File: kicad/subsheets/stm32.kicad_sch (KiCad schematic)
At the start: 11 parts, among them U4 STM32U575RGT6

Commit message: Finalized PMIC and added control from STM32
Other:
- note added: "DEBUG"
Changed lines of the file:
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@@
+		)
+	)
+	(text "DEBUG"
+		(exclude_from_sim no)
+		(at 196.85 62.738 0)
+		(effects
+			(font
+				(size 1.27 1.27)
+			)
+			(justify left)
 		)
 	)
 	(text "RK3566 \nCTRL/DATA"
 		(exclude_from_sim no)
-		(at 202.946 40.894 0)
+		(at 205.486 78.486 0)
 		(effects
 			(font
@@
 	(text "PMIC\n"
 		(exclude_from_sim no)
-		(at 145.542 43.434 0)
+		(at 148.082 81.026 0)
 		(effects
 			(font
@@
 	(text "IMU"
 		(exclude_from_sim no)
-		(at 195.58 64.008 0)
+		(at 198.12 101.6 0)
 		(effects
 			(font
@@
 	(text "FC CTRL"
 		(exclude_from_sim no)
-		(at 153.162 64.516 0)
+		(at 155.702 102.108 0)
 		(effects
 			(font
@@
 	)
 	(image
-		(at 175.26 44.45)
+		(at 177.8 82.042)
 		(data "iVBORw0KGgoAAAANSUhEUgAAAygAAAMVCAIAAAATckfVAAAAA3NCSVQICAjb4U/gAAAgAElEQVR4"
 			"nOzdd1wT9/8H8M8FSEhkBgS1ggFUHLgQ0VYUFATcrbVVXLUuat3a8i0oFQdu0ap11rZWW61aa7EO"

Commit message: Annotations + minor tweaks
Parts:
- renumbered C44 to C41, C45 to C42, C46 to C43, C47 to C44, C48 to C45, C49 to C46, C50 to C47, C51 to C48, C52 to C49, R27 to R26

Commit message: Annotations + minor tweaks
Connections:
- net GND: now also U4.31 (VSS), U4.47 (VSS), U4.63 (VSS)
- net PC15: no longer names the net of U4.4 (PC15)
- net PH0: no longer names the net of U4.5 (PH0)
- net PH1: no longer names the net of U4.6 (PH1)
- no-connect marks 31 -> 34
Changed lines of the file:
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@@
 	(text "PMIC\n"
 		(exclude_from_sim no)
-		(at 33.528 73.914 0)
+		(at 30.988 70.104 0)
 		(effects
 			(font
@@
 	)
 	(junction
-		(at 59.69 36.83)
+		(at 69.85 132.08)
 		(diameter 0)
 		(color 0 0 0 0)
 	)
 	(junction
-		(at 68.58 133.35)
+		(at 59.69 36.83)
 		(diameter 0)
 		(color 0 0 0 0)
@@
 	)
 	(junction
+		(at 52.07 36.83)
+		(diameter 0)
+		(color 0 0 0 0)
+	)
+	(junction
 		(at 72.39 29.21)
 		(diameter 0)
@@
 	)
 	(no_connect
+		(at 52.07 104.14)
+	)
+	(no_connect
 		(at 52.07 76.2)
 	)
@@
 	)
 	(no_connect
+		(at 52.07 53.34)
+	)
+	(no_connect
 		(at 87.63 63.5)
 	)
@@
 	)
 	(no_connect
+		(at 52.07 50.8)
+	)
+	(no_connect
 		(at 52.07 101.6)
 	)
@@
 	(wire
 		(pts
-			(xy 44.45 76.2) (xy 46.99 76.2)
-		)
-		(stroke
-			(width 0)
-			(type default)
-		)
-	)
-	(wire
-		(pts
-			(xy 49.53 53.34) (xy 49.53 78.74)
-		)
-		(stroke
-			(width 0)
-			(type default)
-		)
-	)
-	(wire
-		(pts
 			(xy 35.56 45.72) (xy 35.56 46.99)
 		)
@@
 	(wire
 		(pts
-			(xy 49.53 104.14) (xy 49.53 81.28)
-		)
-		(stroke
-			(width 0)
-			(type default)
-		)
-	)
-	(wire
-		(pts
 			(xy 95.25 50.8) (xy 87.63 50.8)
 		)
@@
 	(wire
 		(pts
-			(xy 52.07 104.14) (xy 49.53 104.14)
-		)
-		(stroke
-			(width 0)
-			(type default)
-		)
-	)
-	(wire
-		(pts
 			(xy 44.45 73.66) (xy 52.07 73.66)
 		)
@@
 	(wire
 		(pts
-			(xy 52.07 50.8) (xy 46.99 50.8)
-		)
-		(stroke
-			(width 0)
-			(type default)
-		)
-	)
-	(wire
-		(pts
-			(xy 46.99 50.8) (xy 46.99 76.2)
-		)
-		(stroke
-			(width 0)
-			(type default)
-		)
-	)
-	(wire
-		(pts
 			(xy 45.72 55.88) (xy 52.07 55.88)
 		)
@@
 	(wire
 		(pts
-			(xy 49.53 78.74) (xy 44.45 78.74)
-		)
-		(stroke
-			(width 0)
-			(type default)
-		)
-	)
-	(wire
-		(pts
 			(xy 64.77 35.56) (xy 64.77 36.83)
 		)
@@
 	(wire
 		(pts
-			(xy 68.58 133.35) (xy 68.58 134.62)
+			(xy 69.85 132.08) (xy 69.85 133.35)
 		)
 		(stroke
@@
 	(wire
 		(pts
+			(xy 69.85 132.08) (xy 71.12 132.08)
+		)
+		(stroke
+			(width 0)
+			(type default)
+		)
+	)
+	(wire
+		(pts
 			(xy 74.93 36.83) (xy 77.47 36.83)
 		)
@@
 	(wire
 		(pts
-			(xy 57.15 36.83) (xy 59.69 36.83)
+			(xy 49.53 36.83) (xy 52.07 36.83)
 		)
 		(stroke
@@
 	(wire
 		(pts
-			(xy 71.12 132.08) (xy 71.12 133.35)
+			(xy 77.47 29.21) (xy 77.47 30.48)
 		)
 		(stroke
@@
 	(wire
 		(pts
-			(xy 52.07 53.34) (xy 49.53 53.34)
+			(xy 52.07 36.83) (xy 59.69 36.83)
 		)
 		(stroke
@@
 	(wire
 		(pts
-			(xy 77.47 29.21) (xy 77.47 30.48)
+			(xy 92.71 121.92) (xy 92.71 114.3)
 		)
 		(stroke
@@
 	(wire
 		(pts
-			(xy 92.71 121.92) (xy 92.71 114.3)
+			(xy 95.25 68.58) (xy 87.63 68.58)
 		)
 		(stroke
@@
 	(wire
 		(pts
-			(xy 95.25 68.58) (xy 87.63 68.58)
+			(xy 59.69 36.83) (xy 64.77 36.83)
 		)
 		(stroke
@@
 	(wire
 		(pts
-			(xy 59.69 36.83) (xy 64.77 36.83)
+			(xy 45.72 45.72) (xy 52.07 45.72)
 		)
 		(stroke
@@
 	(wire
 		(pts
-			(xy 45.72 45.72) (xy 52.07 45.72)
+			(xy 52.07 35.56) (xy 52.07 36.83)
 		)
 		(stroke
@@
 	(wire
 		(pts
-			(xy 68.58 132.08) (xy 68.58 133.35)
-		)
-		(stroke
-			(width 0)
-			(type default)
-		)
-	)
-	(wire
-		(pts
 			(xy 95.25 45.72) (xy 87.63 45.72)
 		)
@@
 	(wire
 		(pts
-			(xy 49.53 81.28) (xy 44.45 81.28)
-		)
-		(stroke
-			(width 0)
-			(type default)
-		)
-	)
-	(wire
-		(pts
 			(xy 87.63 116.84) (xy 95.25 116.84)
 		)
@@
 	(wire
 		(pts
-			(xy 68.58 133.35) (xy 71.12 133.35)
+			(xy 68.58 132.08) (xy 69.85 132.08)
 		)
 		(stroke
@@
 		)
 	)
-	(hierarchical_label "PH1"
-		(shape input)
-		(at 44.45 78.74 180)
-		(effects
-			(font
-				(size 1.27 1.27)
-			)
-			(justify right)
-		)
-	)
 	(hierarchical_label "SWDIO"
 		(shape bidirectional)
@@
 	(hierarchical_label "VDD_3V3"
 		(shape input)
-		(at 57.15 36.83 180)
+		(at 49.53 36.83 180)
 		(effects
 			(font
@@
 		)
 	)
-	(hierarchical_label "PH0"
-		(shape input)
-		(at 44.45 76.2 180)
-		(effects
-			(font
-				(size 1.27 1.27)
-			)
-			(justify right)
-		)
-	)
-	(hierarchical_label "PC15"
-		(shape input)
-		(at 44.45 81.28 180)
-		(effects
-			(font
-				(size 1.27 1.27)
-			)
-			(justify right)
-		)
-	)
 	(hierarchical_label "PB13"
 		(shape input)
@@
 		(on_board yes)
 		(dnp no)
-		(property "Reference" "#PWR034"
+		(property "Reference" "#PWR036"
 			(at 44.45 116.84 0)
 			(effects
@@
 			(project "srad-camera"
 				(path "/da62c771-e8c9-451f-8df1-ec995aadcb11/cf8a0c2d-fb2b-4eaa-949d-0ddbf6dd7299"
-					(reference "#PWR034")
+					(reference "#PWR036")
 					(unit 1)
 				)
@@
 		(on_board yes)
 		(dnp no)
-		(property "Reference" "#PWR033"
+		(property "Reference" "#PWR035"
 			(at 35.56 53.34 0)
 			(effects
@@
 			(project "srad-camera"
 				(path "/da62c771-e8c9-451f-8df1-ec995aadcb11/cf8a0c2d-fb2b-4eaa-949d-0ddbf6dd7299"
-					(reference "#PWR033")
+					(reference "#PWR035")
 					(unit 1)
 				)
@@
 	)
 	(symbol
+		(lib_id "power:PWR_FLAG")
+		(at 52.07 35.56 0)
+		(unit 1)
+		(exclude_from_sim no)
+		(in_bom yes)
+		(on_board yes)
+		(dnp no)
+		(property "Reference" "#FLG02"
+			(at 52.07 33.655 0)
+			(effects
+				(font
+					(size 1.27 1.27)
+				)
+				(hide yes)
+			)
+		)
+		(property "Value" "PWR_FLAG"
+			(at 52.07 31.75 0)
+			(effects
+				(font
+					(size 1.27 1.27)
+				)
+				(hide yes)
+			)
+		)
+		(property "Footprint" ""
+			(at 52.07 35.56 0)
+			(effects
+				(font
+					(size 1.27 1.27)
+				)
+				(hide yes)
+			)
+		)
+		(property "Datasheet" "~"
+			(at 52.07 35.56 0)
+			(effects
+				(font
+					(size 1.27 1.27)
+				)
+				(hide yes)
+			)
+		)
+		(property "Description" "Special symbol for telling ERC where power comes from"
+			(at 52.07 35.56 0)
+			(effects
+				(font
+					(size 1.27 1.27)
+				)
+				(hide yes)
+			)
+		)
+		(pin "1"
+		)
+		(instances
+			(project "srad-camera"
+				(path "/da62c771-e8c9-451f-8df1-ec995aadcb11/cf8a0c2d-fb2b-4eaa-949d-0ddbf6dd7299"
+					(reference "#FLG02")
+					(unit 1)
+				)
+			)
+		)
+	)
+	(symbol
 		(lib_id "power:GND")
-		(at 68.58 134.62 0)
+		(at 69.85 133.35 0)
 		(unit 1)
 		(exclude_from_sim no)
@@
 		(on_board yes)
 		(dnp no)
-		(fields_autoplaced yes)
-		(property "Reference" "#PWR035"
-			(at 68.58 140.97 0)
+		(property "Reference" "#PWR037"
+			(at 69.85 139.7 0)
 			(effects
 				(font
@@
 		)
 		(property "Value" "GND"
-			(at 68.58 139.7 0)
+			(at 69.85 137.16 0)
 			(effects
 				(font
@@
 		)
 		(property "Footprint" ""
-			(at 68.58 134.62 0)
+			(at 69.85 133.35 0)
 			(effects
 				(font
@@
 		)
 		(property "Datasheet" ""
-			(at 68.58 134.62 0)
+			(at 69.85 133.35 0)
 			(effects
 				(font
@@
 		)
 		(property "Description" "Power symbol creates a global label with name \"GND\" , ground"
-			(at 68.58 134.62 0)
+			(at 69.85 133.35 0)
 			(effects
 				(font
@@
 			(project "srad-camera"
 				(path "/da62c771-e8c9-451f-8df1-ec995aadcb11/cf8a0c2d-fb2b-4eaa-949d-0ddbf6dd7299"
-					(reference "#PWR035")
+					(reference "#PWR037")
 					(unit 1)
 				)
@@
 		(on_board yes)
 		(dnp no)
-		(property "Reference" "#PWR032"
+		(property "Reference" "#PWR034"
 			(at 82.55 38.1 0)
 			(effects
@@
 			(project ""
 				(path "/da62c771-e8c9-451f-8df1-ec995aadcb11/cf8a0c2d-fb2b-4eaa-949d-0ddbf6dd7299"
-					(reference "#PWR032")
+					(reference "#PWR034")
 					(unit 1)
 				)

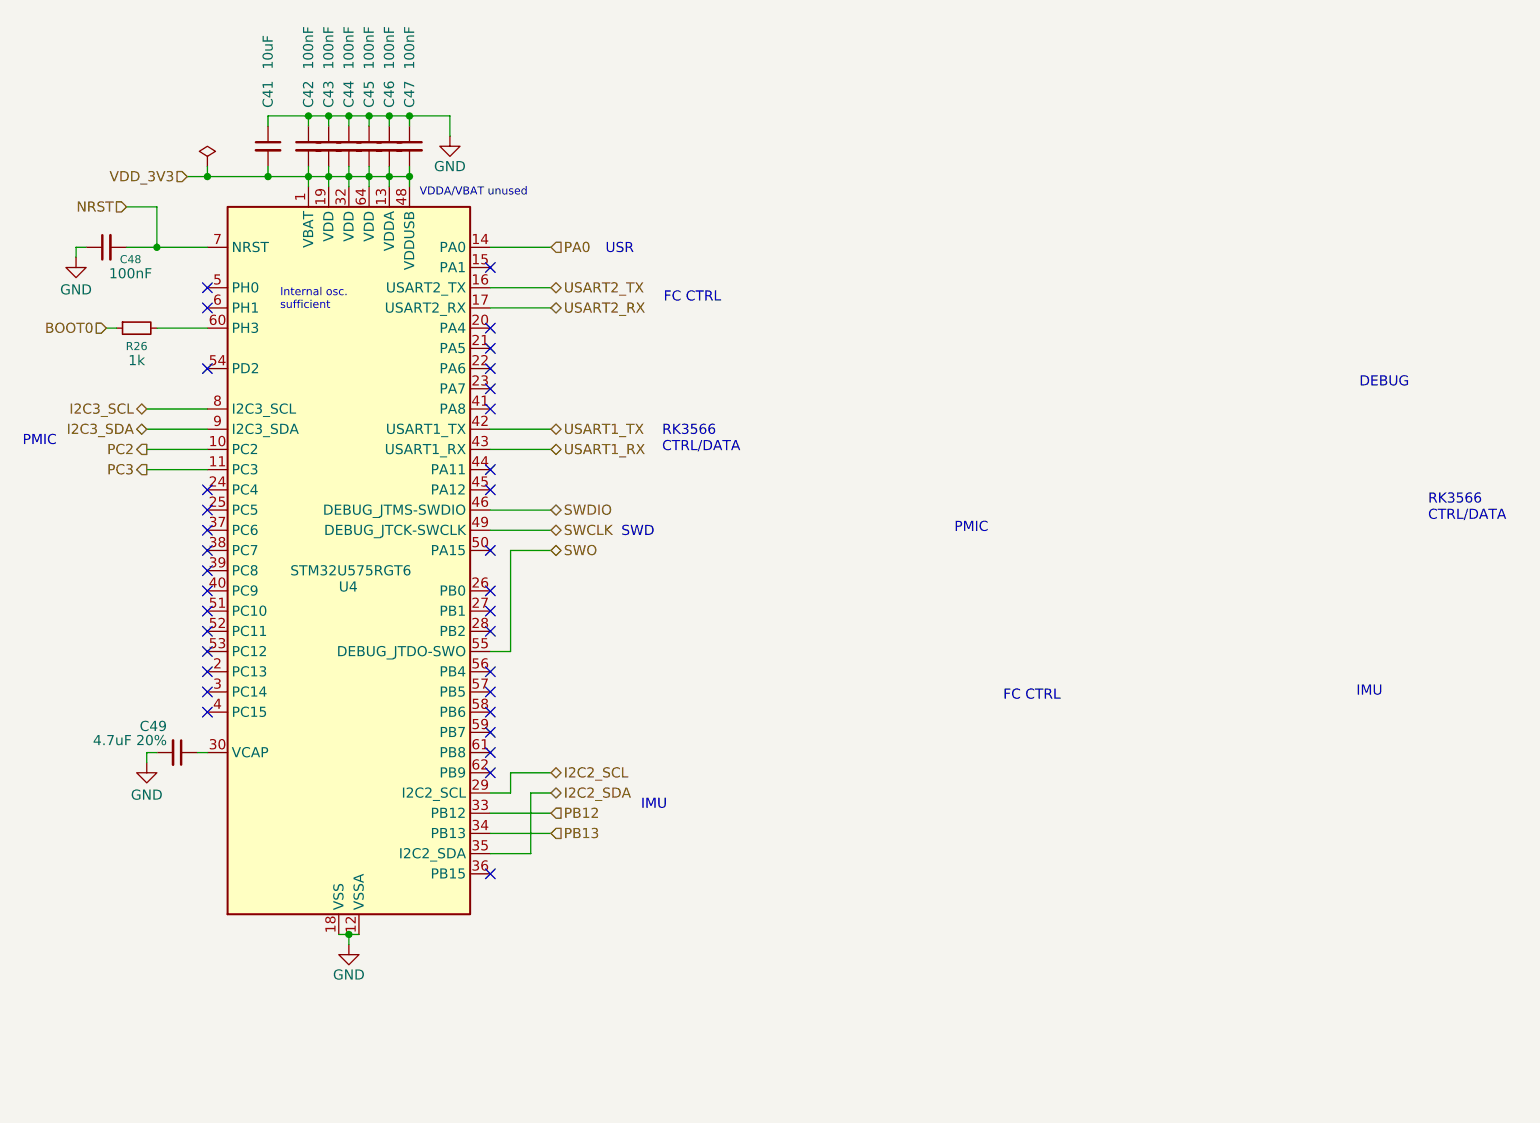
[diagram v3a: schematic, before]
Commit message: Change all sheets to A4, name sheets, split RK3566 into hierarchy
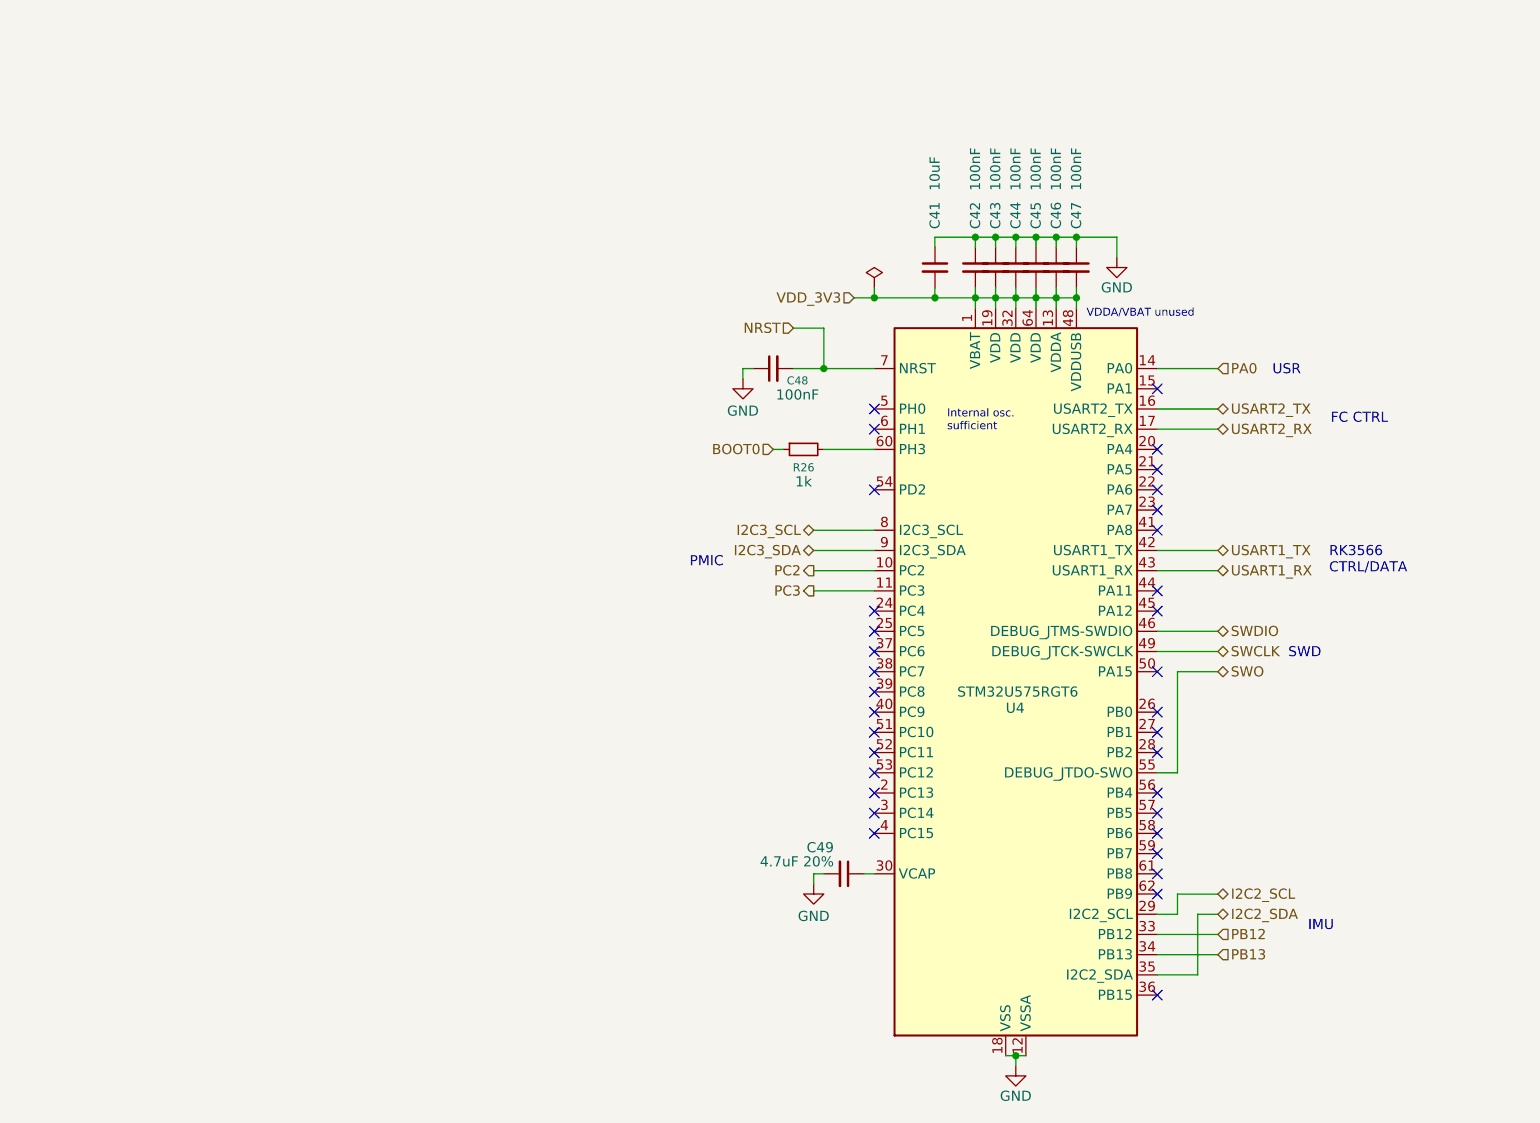
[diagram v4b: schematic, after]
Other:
- note removed: "DEBUG"
- title: (none) -> STM32U575RGT6 Microcontroller
- moved on the sheet: C41, C42, C43, C44, C45, C46, C47, C48, C49, R26, U4

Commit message: Mark as R1.0
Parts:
- renumbered C41 to C42, C42 to C43, C43 to C44, C44 to C45, C45 to C46, C46 to C47, C47 to C48, C48 to C49, C49 to C50, R26 to R28
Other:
- company: (none) -> UVic Rocketry
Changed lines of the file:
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@@
 	(title_block
 		(title "STM32U575RGT6 Microcontroller")
+		(date "2025-11-23")
+		(rev "1.0")
+		(company "UVic Rocketry")
+		(comment 1 "Author: Eric Handley")
 	)
 	(text "IMU"
@@
 		(on_board yes)
 		(dnp no)
-		(property "Reference" "#PWR036"
+		(property "Reference" "#PWR043"
 			(at 128.27 132.08 0)
 			(effects
@@
 			(project "srad-camera"
 				(path "/da62c771-e8c9-451f-8df1-ec995aadcb11/cf8a0c2d-fb2b-4eaa-949d-0ddbf6dd7299"
-					(reference "#PWR036")
+					(reference "#PWR043")
 					(unit 1)
 				)
@@
 		(on_board yes)
 		(dnp no)
-		(property "Reference" "C45"
+		(property "Reference" "C46"
 			(at 156.21 43.434 90)
 			(effects
@@
 			(project "srad-camera"
 				(path "/da62c771-e8c9-451f-8df1-ec995aadcb11/cf8a0c2d-fb2b-4eaa-949d-0ddbf6dd7299"
-					(reference "C45")
+					(reference "C46")
 					(unit 1)
 				)
@@
 		(on_board yes)
 		(dnp no)
-		(property "Reference" "C44"
+		(property "Reference" "C45"
 			(at 153.67 43.434 90)
 			(effects
@@
 			(project "srad-camera"
 				(path "/da62c771-e8c9-451f-8df1-ec995aadcb11/cf8a0c2d-fb2b-4eaa-949d-0ddbf6dd7299"
-					(reference "C44")
+					(reference "C45")
 					(unit 1)
 				)
@@
 		(on_board yes)
 		(dnp no)
-		(property "Reference" "C48"
+		(property "Reference" "C49"
 			(at 126.238 62.484 90)
 			(effects
@@
 			(project "srad-camera"
 				(path "/da62c771-e8c9-451f-8df1-ec995aadcb11/cf8a0c2d-fb2b-4eaa-949d-0ddbf6dd7299"
-					(reference "C48")
+					(reference "C49")
 					(unit 1)
 				)
@@
 		(on_board yes)
 		(dnp no)
-		(property "Reference" "C42"
+		(property "Reference" "C43"
 			(at 148.59 43.434 90)
 			(effects
@@
 			(project "srad-camera"
 				(path "/da62c771-e8c9-451f-8df1-ec995aadcb11/cf8a0c2d-fb2b-4eaa-949d-0ddbf6dd7299"
-					(reference "C42")
+					(reference "C43")
 					(unit 1)
 				)
@@
 		(on_board yes)
 		(dnp no)
-		(property "Reference" "#PWR035"
+		(property "Reference" "#PWR042"
 			(at 119.38 68.58 0)
 			(effects
@@
 			(project "srad-camera"
 				(path "/da62c771-e8c9-451f-8df1-ec995aadcb11/cf8a0c2d-fb2b-4eaa-949d-0ddbf6dd7299"
-					(reference "#PWR035")
+					(reference "#PWR042")
 					(unit 1)
 				)
@@
 		(on_board yes)
 		(dnp no)
-		(property "Reference" "C47"
+		(property "Reference" "C48"
 			(at 161.29 43.434 90)
 			(effects
@@
 			(project "srad-camera"
 				(path "/da62c771-e8c9-451f-8df1-ec995aadcb11/cf8a0c2d-fb2b-4eaa-949d-0ddbf6dd7299"
-					(reference "C47")
+					(reference "C48")
 					(unit 1)
 				)
@@
 		(on_board yes)
 		(dnp no)
-		(property "Reference" "C43"
+		(property "Reference" "C44"
 			(at 151.13 43.434 90)
 			(effects
@@
 			(project "srad-camera"
 				(path "/da62c771-e8c9-451f-8df1-ec995aadcb11/cf8a0c2d-fb2b-4eaa-949d-0ddbf6dd7299"
-					(reference "C43")
+					(reference "C44")
 					(unit 1)
 				)
@@
 		(on_board yes)
 		(dnp no)
-		(property "Reference" "C41"
+		(property "Reference" "C42"
 			(at 143.51 43.434 90)
 			(effects
@@
 			(project "srad-camera"
 				(path "/da62c771-e8c9-451f-8df1-ec995aadcb11/cf8a0c2d-fb2b-4eaa-949d-0ddbf6dd7299"
-					(reference "C41")
+					(reference "C42")
 					(unit 1)
 				)
@@
 		(on_board yes)
 		(dnp no)
-		(property "Reference" "C49"
+		(property "Reference" "C50"
 			(at 130.81 121.158 90)
 			(effects
@@
 			(project "srad-camera"
 				(path "/da62c771-e8c9-451f-8df1-ec995aadcb11/cf8a0c2d-fb2b-4eaa-949d-0ddbf6dd7299"
-					(reference "C49")
+					(reference "C50")
 					(unit 1)
 				)
@@
 		(on_board yes)
 		(dnp no)
-		(property "Reference" "#FLG02"
+		(property "Reference" "#FLG03"
 			(at 135.89 48.895 0)
 			(effects
@@
 			(project "srad-camera"
 				(path "/da62c771-e8c9-451f-8df1-ec995aadcb11/cf8a0c2d-fb2b-4eaa-949d-0ddbf6dd7299"
-					(reference "#FLG02")
+					(reference "#FLG03")
 					(unit 1)
 				)
@@
 		(on_board yes)
 		(dnp no)
-		(property "Reference" "#PWR037"
+		(property "Reference" "#PWR044"
 			(at 153.67 154.94 0)
 			(effects
@@
 			(project "srad-camera"
 				(path "/da62c771-e8c9-451f-8df1-ec995aadcb11/cf8a0c2d-fb2b-4eaa-949d-0ddbf6dd7299"
-					(reference "#PWR037")
+					(reference "#PWR044")
 					(unit 1)
 				)
@@
 		(on_board yes)
 		(dnp no)
-		(property "Reference" "#PWR034"
+		(property "Reference" "#PWR041"
 			(at 166.37 53.34 0)
 			(effects
@@
 			(project ""
 				(path "/da62c771-e8c9-451f-8df1-ec995aadcb11/cf8a0c2d-fb2b-4eaa-949d-0ddbf6dd7299"
-					(reference "#PWR034")
+					(reference "#PWR041")
 					(unit 1)
 				)
@@
 		(on_board yes)
 		(dnp no)
-		(property "Reference" "R26"
+		(property "Reference" "R28"
 			(at 127 73.406 90)
 			(effects
@@
 			(project "srad-camera"
 				(path "/da62c771-e8c9-451f-8df1-ec995aadcb11/cf8a0c2d-fb2b-4eaa-949d-0ddbf6dd7299"
-					(reference "R26")
+					(reference "R28")
 					(unit 1)
 				)
@@
 		(on_board yes)
 		(dnp no)
-		(property "Reference" "C46"
+		(property "Reference" "C47"
 			(at 158.75 43.434 90)
 			(effects
@@
 			(project "srad-camera"
 				(path "/da62c771-e8c9-451f-8df1-ec995aadcb11/cf8a0c2d-fb2b-4eaa-949d-0ddbf6dd7299"
-					(reference "C46")
+					(reference "C47")
 					(unit 1)
 				)
